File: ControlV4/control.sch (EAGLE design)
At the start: 49 parts, among them P1 CONNEC_1X03, P10 CONNEC_1X03, P11 CONNEC_1X03, P12 CONNEC_1X03, P2 CONNEC_1X03, P3 CONNEC_1X03, P4 CONNEC_1X03, P5 CONNEC_1X03, P6 CONNEC_1X03, P7 CONNEC_1X03, P8 CONNEC_1X03, P9 CONNEC_1X03

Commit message: V4
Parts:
- removed JP1: (no value), pinhead:PINHD-1X3
- added C7, C8: (no value), SparkFun-Capacitors:CAP_POLPTH2
- added JP: CONNEC_1X03, RobotCampus:CONNEC_1X03
- XB1: value XBEE-PRO -> XBEE; device maxstream:XBEE-PRO -> RobotCampus:XBEE
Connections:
- net 3.3: now also C8.+
- net GND: now also C7.-, C8.-
- net NET1: now also JP.1; no longer JP1.3
- net VCC_IN: now also JP.3; no longer JP1.1
- net VPOWER: now also C7.+, JP.2; no longer JP1.2
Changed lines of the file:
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@@
 <class number="0" name="default" width="0" drill="0">
 </class>
-<class number="1" name="alime" width="1.143" drill="0">
+<class number="1" name="alime" width="1.016" drill="0">
 </class>
 </classes>
@@
 <part name="R14" library="rcl" deviceset="R-EU_" device="R0805"/>
 <part name="GND12" library="supply1" deviceset="GND" device=""/>
-<part name="XB1" library="maxstream" deviceset="XBEE" device="-PRO"/>
+<part name="XB1" library="RobotCampus" deviceset="XBEE" device=""/>
 <part name="GND16" library="supply1" deviceset="GND" device=""/>
-<part name="JP1" library="pinhead" deviceset="PINHD-1X3" device=""/>
 <part name="U$2" library="RobotCampus" deviceset="CONNEC_1X03" device=""/>
 <part name="U$3" library="RobotCampus" deviceset="DIODE254" device=""/>
@@
 <part name="GND7" library="supply1" deviceset="GND" device=""/>
 <part name="U$5" library="RobotCampus" deviceset="DIODE" device="TO252AA"/>
+<part name="JP" library="RobotCampus" deviceset="CONNEC_1X03" device=""/>
+<part name="C7" library="SparkFun-Capacitors" deviceset="CAP_POL" device="PTH2"/>
+<part name="GND17" library="supply1" deviceset="GND" device=""/>
+<part name="C8" library="SparkFun-Capacitors" deviceset="CAP_POL" device="PTH2"/>
+<part name="GND18" library="supply1" deviceset="GND" device=""/>
 </parts>
 <sheets>
@@
 <instance part="XB1" gate="G$1" x="154.94" y="0"/>
 <instance part="GND16" gate="1" x="129.54" y="-35.56"/>
-<instance part="JP1" gate="A" x="187.96" y="170.18" rot="MR180"/>
 <instance part="U$2" gate="G$1" x="104.14" y="-15.24"/>
 <instance part="U$3" gate="G$1" x="91.44" y="142.24"/>
@@
 <instance part="GND7" gate="1" x="129.54" y="139.7"/>
 <instance part="U$5" gate="G$1" x="160.02" y="172.72"/>
+<instance part="JP" gate="G$1" x="182.88" y="167.64"/>
+<instance part="C7" gate="G$1" x="228.6" y="152.4"/>
+<instance part="GND17" gate="1" x="228.6" y="142.24"/>
+<instance part="C8" gate="G$1" x="284.48" y="152.4"/>
+<instance part="GND18" gate="1" x="284.48" y="142.24"/>
 </instances>
 <busses>
@@
 <wire x1="129.54" y1="144.78" x2="129.54" y2="142.24" width="0.1524" layer="91"/>
 </segment>
+<segment>
+<pinref part="GND17" gate="1" pin="GND"/>
+<pinref part="C7" gate="G$1" pin="-"/>
+<wire x1="228.6" y1="144.78" x2="228.6" y2="147.32" width="0.1524" layer="91"/>
+</segment>
+<segment>
+<pinref part="GND18" gate="1" pin="GND"/>
+<pinref part="C8" gate="G$1" pin="-"/>
+<wire x1="284.48" y1="144.78" x2="284.48" y2="147.32" width="0.1524" layer="91"/>
+</segment>
 </net>
 <net name="PWM7" class="0">
@@
 <wire x1="223.52" y1="154.94" x2="218.44" y2="154.94" width="0.1524" layer="91"/>
 <pinref part="C4" gate="G$1" pin="+"/>
-</segment>
-<segment>
-<pinref part="JP1" gate="A" pin="2"/>
+<pinref part="C7" gate="G$1" pin="+"/>
+<wire x1="228.6" y1="154.94" x2="223.52" y2="154.94" width="0.1524" layer="91"/>
+</segment>
+<segment>
 <wire x1="185.42" y1="170.18" x2="198.12" y2="170.18" width="0.1524" layer="91"/>
 <label x="198.12" y="170.18" size="1.778" layer="95"/>
+<pinref part="JP" gate="G$1" pin="2"/>
 </segment>
 <segment>
@@
 </segment>
 </net>
-<net name="VCC_IN" class="0">
+<net name="VCC_IN" class="1">
 <segment>
 <pinref part="JST_IN" gate="G$1" pin="VCC"/>
@@
 </segment>
 <segment>
-<pinref part="JP1" gate="A" pin="1"/>
 <wire x1="185.42" y1="167.64" x2="172.72" y2="167.64" width="0.1524" layer="91"/>
 <label x="172.72" y="167.64" size="1.778" layer="95"/>
+<pinref part="JP" gate="G$1" pin="3"/>
 </segment>
 <segment>
@@
 <segment>
 <label x="162.56" y="170.18" size="1.778" layer="95"/>
-<pinref part="JP1" gate="A" pin="3"/>
 <wire x1="160.02" y1="172.72" x2="185.42" y2="172.72" width="0.1524" layer="91"/>
 <pinref part="U$5" gate="G$1" pin="C"/>
+<pinref part="JP" gate="G$1" pin="1"/>
 </segment>
 </net>
@@
 <wire x1="276.86" y1="154.94" x2="276.86" y2="157.48" width="0.1524" layer="91"/>
 <label x="276.86" y="157.48" size="1.778" layer="95"/>
-</segment>
-<segment>
+<pinref part="C8" gate="G$1" pin="+"/>
+<wire x1="284.48" y1="154.94" x2="276.86" y2="154.94" width="0.1524" layer="91"/>
+</segment>
+<segment>

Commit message: V4
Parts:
- removed JST_IN, JST_MICRO: JST_2, perso:JST_2
- added U$10, U$11: JST_2, RobotCampus:JST_2
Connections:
- net GND: now also U$10.GND, U$11.GND; no longer JST_IN.GND, JST_MICRO.GND
- net VCC_IN: now also U$11.VCC; no longer JST_IN.VCC
- net VMICRO: now also U$10.VCC; no longer JST_MICRO.VCC
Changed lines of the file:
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@@
 <part name="C2" library="rcl" deviceset="C-EU" device="075-032X103"/>
 <part name="GND15" library="supply1" deviceset="GND" device=""/>
-<part name="JST_IN" library="perso" deviceset="JST_2" device=""/>
-<part name="JST_MICRO" library="perso" deviceset="JST_2" device=""/>
 <part name="R13" library="rcl" deviceset="R-EU_" device="R0805"/>
 <part name="R14" library="rcl" deviceset="R-EU_" device="R0805"/>
@@
 <part name="C8" library="SparkFun-Capacitors" deviceset="CAP_POL" device="PTH2"/>
 <part name="GND18" library="supply1" deviceset="GND" device=""/>
+<part name="U$10" library="RobotCampus" deviceset="JST_2" device=""/>
+<part name="U$11" library="RobotCampus" deviceset="JST_2" device=""/>
 </parts>
 <sheets>
@@
 <instance part="C2" gate="G$1" x="218.44" y="152.4"/>
 <instance part="GND15" gate="1" x="58.42" y="127"/>
-<instance part="JST_IN" gate="G$1" x="73.66" y="132.08"/>
-<instance part="JST_MICRO" gate="G$1" x="73.66" y="152.4"/>
 <instance part="R13" gate="G$1" x="45.72" y="91.44"/>
 <instance part="R14" gate="G$1" x="53.34" y="86.36" rot="R90"/>
@@
 <instance part="C8" gate="G$1" x="284.48" y="152.4"/>
 <instance part="GND18" gate="1" x="284.48" y="142.24"/>
+<instance part="U$10" gate="G$1" x="73.66" y="152.4"/>
+<instance part="U$11" gate="G$1" x="73.66" y="132.08"/>
 </instances>
 <busses>
@@
 <pinref part="GND5" gate="1" pin="GND"/>
 <wire x1="58.42" y1="149.86" x2="58.42" y2="147.32" width="0.1524" layer="91"/>
-<pinref part="JST_MICRO" gate="G$1" pin="GND"/>
+<pinref part="U$10" gate="G$1" pin="GND"/>
 </segment>
 <segment>
@@
 <segment>
 <pinref part="GND15" gate="1" pin="GND"/>
-<pinref part="JST_IN" gate="G$1" pin="GND"/>
 <wire x1="58.42" y1="129.54" x2="63.5" y2="129.54" width="0.1524" layer="91"/>
+<pinref part="U$11" gate="G$1" pin="GND"/>
 </segment>
 <segment>
@@
 <net name="VCC_IN" class="1">
 <segment>
-<pinref part="JST_IN" gate="G$1" pin="VCC"/>
 <wire x1="63.5" y1="134.62" x2="58.42" y2="134.62" width="0.1524" layer="91"/>
 <label x="50.8" y="134.62" size="1.778" layer="95"/>
+<pinref part="U$11" gate="G$1" pin="VCC"/>
 </segment>
 <segment>
@@
 <segment>
 <wire x1="63.5" y1="154.94" x2="58.42" y2="154.94" width="0.1524" layer="91"/>
-<pinref part="JST_MICRO" gate="G$1" pin="VCC"/>
 <label x="58.42" y="157.48" size="1.778" layer="95" rot="R180"/>
-</segment>
-<segment>
+<pinref part="U$10" gate="G$1" pin="VCC"/>
+</segment>
+<segment>

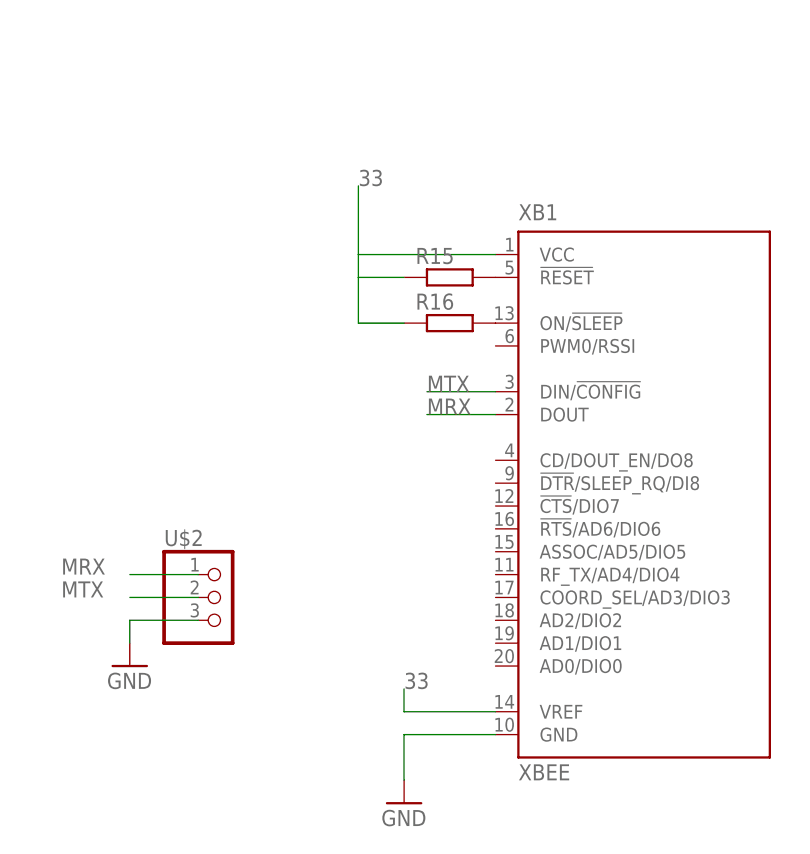
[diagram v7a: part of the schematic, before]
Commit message: Fixing the 33/3.3 problem
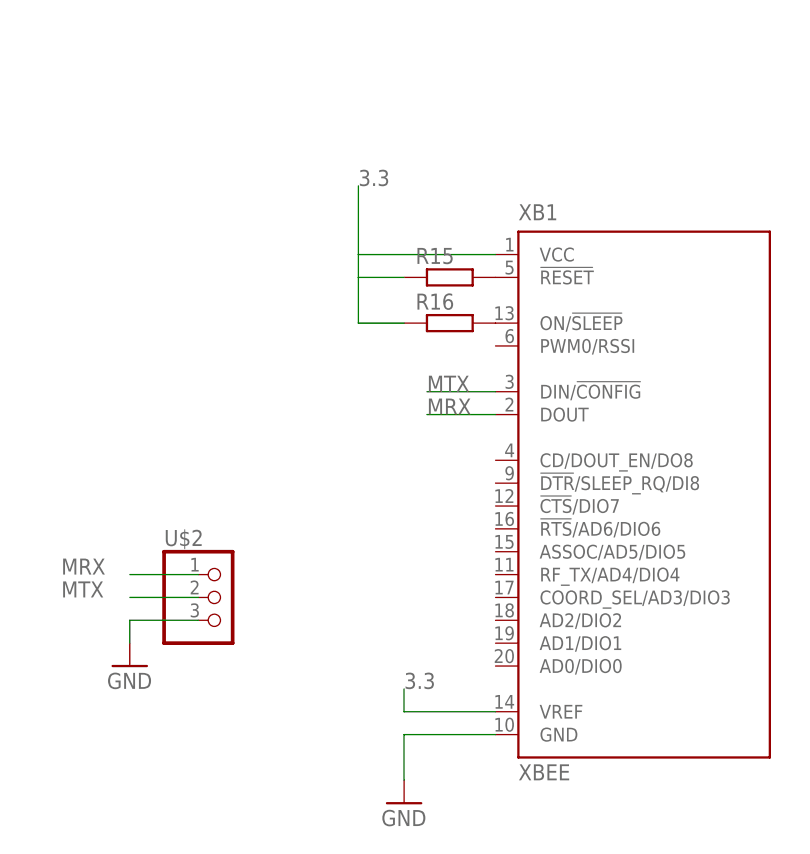
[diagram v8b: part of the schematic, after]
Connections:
- removed net 33: R15.1, R16.1, XB1.VCC, XB1.VREF
- net 3.3: now also R15.1, R16.1, XB1.VCC, XB1.VREF
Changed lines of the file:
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@@
-</segment>
-</net>
-<net name="33" class="0">
-<segment>
-<pinref part="XB1" gate="G$1" pin="VCC"/>
-<wire x1="139.7" y1="25.4" x2="124.46" y2="25.4" width="0.1524" layer="91"/>
-<wire x1="124.46" y1="25.4" x2="124.46" y2="33.02" width="0.1524" layer="91"/>
-<label x="124.46" y="33.02" size="1.778" layer="95"/>
-<pinref part="R15" gate="G$1" pin="1"/>
-<wire x1="129.54" y1="22.86" x2="124.46" y2="22.86" width="0.1524" layer="91"/>
-<wire x1="124.46" y1="22.86" x2="124.46" y2="25.4" width="0.1524" layer="91"/>
-<pinref part="R16" gate="G$1" pin="1"/>
-<wire x1="129.54" y1="17.78" x2="124.46" y2="17.78" width="0.1524" layer="91"/>
-<wire x1="124.46" y1="17.78" x2="124.46" y2="22.86" width="0.1524" layer="91"/>
-</segment>
-<segment>
-<pinref part="XB1" gate="G$1" pin="VREF"/>
-<wire x1="139.7" y1="-25.4" x2="129.54" y2="-25.4" width="0.1524" layer="91"/>
-<wire x1="129.54" y1="-25.4" x2="129.54" y2="-22.86" width="0.1524" layer="91"/>
-<label x="129.54" y="-22.86" size="1.778" layer="95"/>
 </segment>
 </net>
@@
 <label x="170.18" y="149.86" size="1.778" layer="95"/>
 </segment>
+<segment>
+<pinref part="XB1" gate="G$1" pin="VCC"/>
+<wire x1="139.7" y1="25.4" x2="124.46" y2="25.4" width="0.1524" layer="91"/>
+<wire x1="124.46" y1="25.4" x2="124.46" y2="33.02" width="0.1524" layer="91"/>
+<label x="124.46" y="33.02" size="1.778" layer="95"/>
+<pinref part="R15" gate="G$1" pin="1"/>
+<wire x1="129.54" y1="22.86" x2="124.46" y2="22.86" width="0.1524" layer="91"/>
+<wire x1="124.46" y1="22.86" x2="124.46" y2="25.4" width="0.1524" layer="91"/>
+<pinref part="R16" gate="G$1" pin="1"/>
+<wire x1="129.54" y1="17.78" x2="124.46" y2="17.78" width="0.1524" layer="91"/>
+<wire x1="124.46" y1="17.78" x2="124.46" y2="22.86" width="0.1524" layer="91"/>
+</segment>
+<segment>
+<pinref part="XB1" gate="G$1" pin="VREF"/>
+<wire x1="139.7" y1="-25.4" x2="129.54" y2="-25.4" width="0.1524" layer="91"/>
+<wire x1="129.54" y1="-25.4" x2="129.54" y2="-22.86" width="0.1524" layer="91"/>
+<label x="129.54" y="-22.86" size="1.778" layer="95"/>
+</segment>
 </net>
